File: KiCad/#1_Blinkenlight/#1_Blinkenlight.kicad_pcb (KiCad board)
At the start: 2 copper layers, 52.3 x 21.5 mm, 18 parts, among them J1 Conn_02x19_Odd_Even

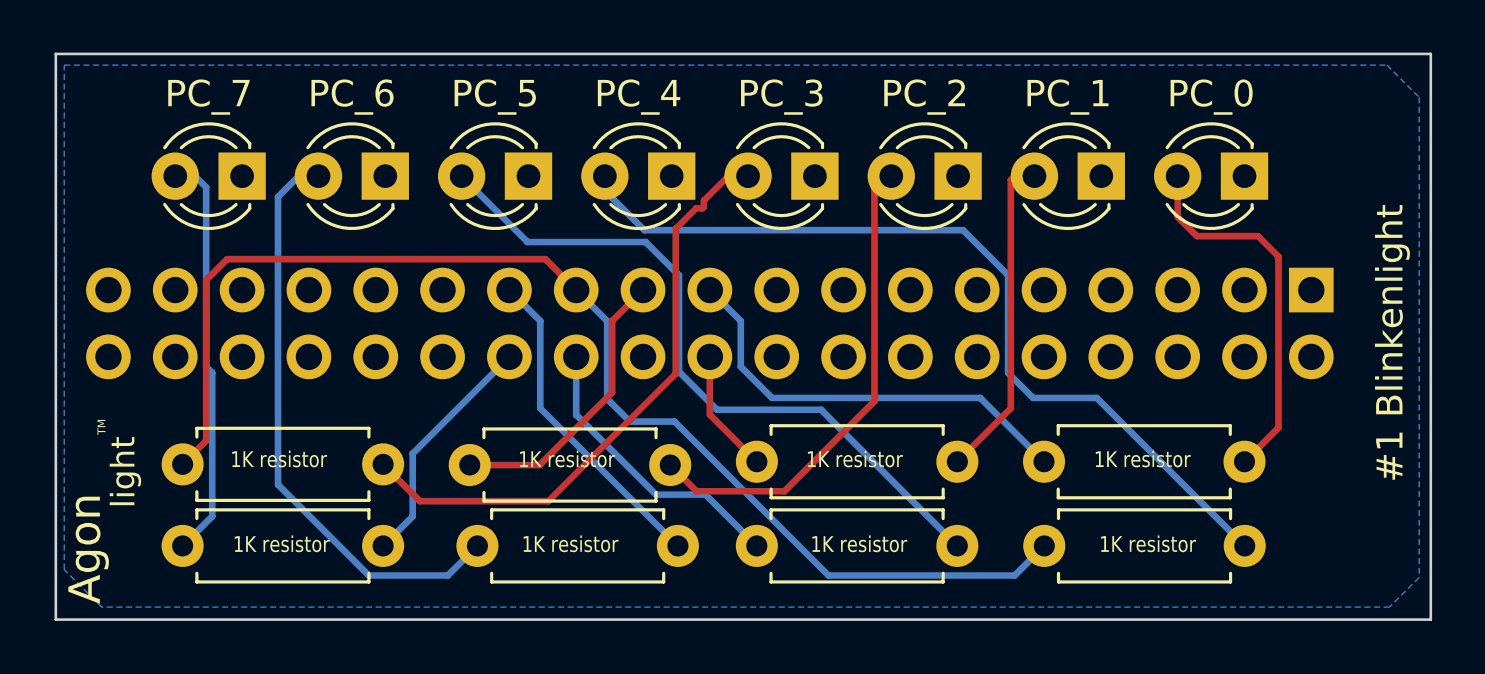
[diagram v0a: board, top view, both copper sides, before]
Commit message: Blinkenlight schematic correction
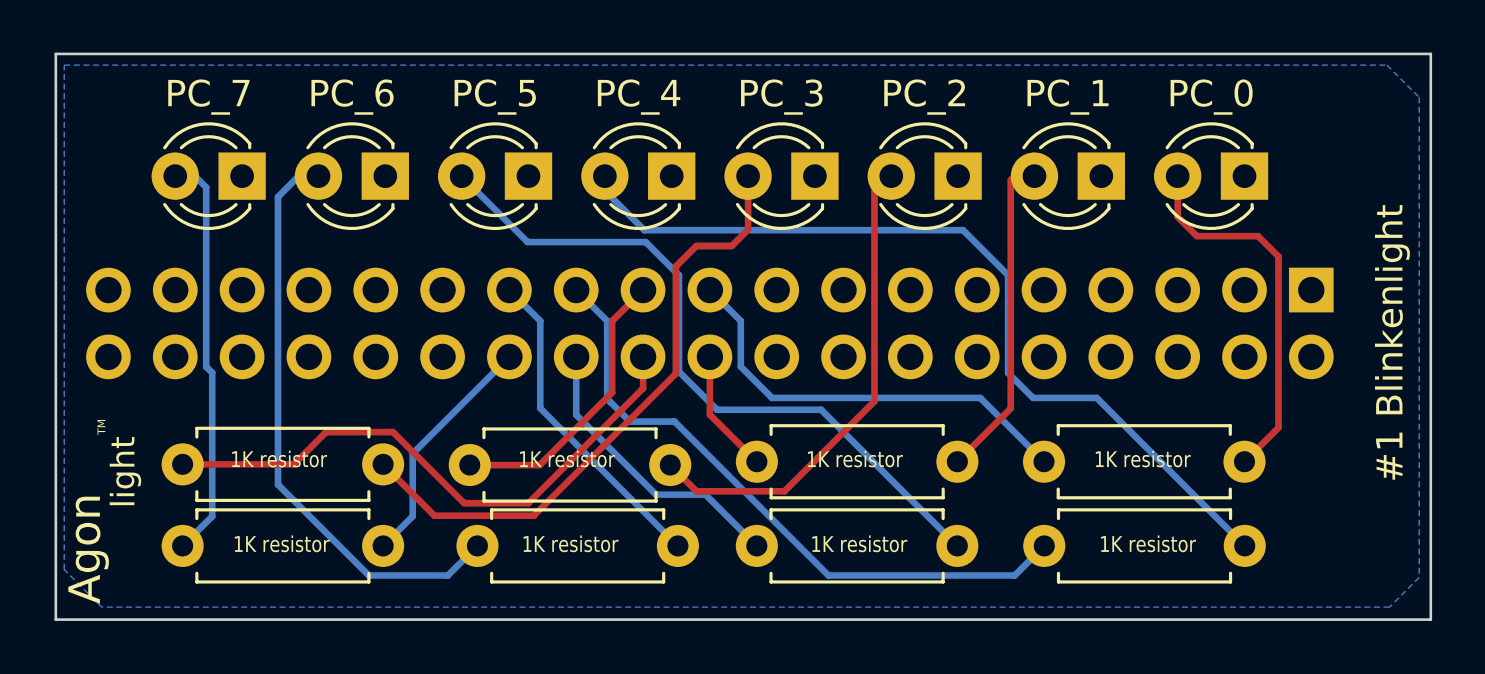
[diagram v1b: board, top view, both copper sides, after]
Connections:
- R3 pad 1: GPIO_PC4 -> GPIO_PC3
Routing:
- net GPIO_PC4: track 46.7 -> 24.5 mm
- net GPIO_PC3: track 0.00 -> 22.1 mm
- net Net-(PC_3-Pad2): track 23.2 -> 24.4 mm
